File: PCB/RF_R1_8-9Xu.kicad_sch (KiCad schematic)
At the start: 30 parts, among them J1 JST, J2 JST, SW1 BOOT0, U1 STM32F401CBUx, U2 XC6206PxxxMR, Y1 8 MHz

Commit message: Update and pre-production output
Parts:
- C1: LCSC (none) -> C23733
- C2, C3, C9: LCSC (none) -> C52923
- C4, C5, C6, C7, C8: LCSC (none) -> C307331
- D1: LCSC (none) -> C2827688
- F1: LCSC (none) -> C70076
- J1: LCSC (none) -> C265068
- J2: LCSC (none) -> C145956
- R1, R2: LCSC (none) -> C25905
- R10, R11, R12: LCSC (none) -> C25744
- R3, R4, R5, R6, R7, R9: LCSC (none) -> C25076
- R8: LCSC (none) -> C25741
- SW1: footprint Connector_PinHeader_2.54mm:PinHeader_1x02_P2.54mm_Vertical -> Connector_PinHeader_1.27mm:PinHeader_1x02_P1.27mm_Vertical
- U1: LCSC (none) -> C118825
- U2: LCSC (none) -> C5446
- USB1: LCSC (none) -> C165948
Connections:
- net AMUX_SEL_0: now also U1.40 (PB4); no longer U1.42 (PB6)
- net AMUX_SEL_2: now also U1.42 (PB6); no longer U1.40 (PB4)
- net APLEX_EN_PIN_1: now also U1.16 (PA6); no longer U1.39 (PB3)
- net D+: now also D1.3 (I/O2); no longer D1.2 (I/O1)
- net D-: now also D1.2 (I/O1); no longer D1.3 (I/O2)
- net DISCHARGE_PIN: now also U1.14 (PA4); no longer U1.16 (PA6)
- net ROW2: now also R9.1; no longer R3.2
- net ROW3: now also R4.1; no longer R5.2
- net ROW4: now also R5.2; no longer R4.1, R9.1
- net at R3.1: now also U1.25 (PB12); no longer U1.18 (PB0)
- net at R9.2: now also U1.27 (PB14)
- net at U1.17 (PA7): no longer R5.1
- net at U1.19 (PB1): no longer R4.2
- net at U1.26 (PB13): now also R4.2
- net at U1.28 (PB15): now also R5.1
- new net ROW5: R3.2
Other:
- moved on the sheet: R3, R4, R5, R9

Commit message: Final PCB Rev
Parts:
- added J3: Conn_01x03, Connector_PinHeader_2.00mm:PinHeader_1x03_P2.00mm_Vertical, symbol Connector_Generic:Conn_01x03
- added J4: Conn_01x03, cipulot_parts:LED_Strip_Pad, symbol Connector_Generic:Conn_01x03
- added U6: SN74AHCT1G125, Package_TO_SOT_SMD:SOT-23-5, symbol cipulot_parts:SN74AHCT1G125
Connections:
- net +5V: now also J3.3 (Pin_3), J4.3 (Pin_3), U6.5 (VCC)
- net GND: now also J3.1 (Pin_1), J4.1 (Pin_1), U6.1 (~{OE}), U6.3 (GND)
- net LED_3V3: now reaches U1.38 (PA15)
- net LED_3V3: now also U6.2 (A)
- new net LED_5V: J3.2 (Pin_2), J4.2 (Pin_2), U6.4 (B)
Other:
- note added: "LED Logic Level Shifter"
- note added: "LED Strip Connector"
- note added: "SMD"
- note added: "THT"
- moved on the sheet: Y1

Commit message: Fix PA9 being used
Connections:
- net at R3.1: now also U1.18 (PB0); no longer U1.25 (PB12)
- net at R6.2: now also U1.28 (PB15); no longer U1.29 (PA8)
- net at R7.1: now also U1.29 (PA8); no longer U1.30 (PA9)
- net at R9.2: now also U1.26 (PB13); no longer U1.27 (PB14)
- net at R4.2: now also U1.25 (PB12); no longer U1.26 (PB13)
- net at R5.1: now also U1.27 (PB14); no longer U1.28 (PB15)
- no-connect marks 2 -> 3
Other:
- moved on the sheet: R3, R4, R5, R6, R7, R9

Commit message: Production files update
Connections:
- no-connect marks 3 -> 16
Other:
- note added: "DO NOT USE"
- note added: "MCU"
- note added: "NOTE"
- note added: "The board is designed around the STM32F4 family of MCUs to allow for easy swap in case a specific SKU is OOS. Here follows a list of tested (by myself) MCUs: - STM32F4 - SMT32F4 - SMT32F4"
- moved on the sheet: C1, R3, R4, R5, R6, R7, R8, R9

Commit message: Update of PCB
Added shielding copper pad for plate electrical connection, along with EMI filtering through capacitor and inductor.
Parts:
- added C1: 100n, Capacitor_SMD:C_0603_1608Metric, symbol Device:C
- added L1: 220 @ 100MHz, 2A, Inductor_SMD:L_0603_1608Metric, symbol Device:L
- renumbered C9 to C10, C1 to C2, C2 to C3, C3 to C4, C4 to C5, C5 to C6, C6 to C7, C7 to C8, C8 to C9, R7 to R4, R8 to R5, R4 to R6, R9 to R7, R5 to R8, R6 to R9, U6 to U2, U2 to U3
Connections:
- net GND: now also C1.2, L1.2
- new net GNDPWR: C1.1, L1.1
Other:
- note added: "The board is designed around the STM32F4 family of MCUs to allow for easy swap in case a specific SKU is OOS. Here follows a list of tested (by myself) MCUs: - STM32F401CBU"
- note removed: "The board is designed around the STM32F4 family of MCUs to allow for easy swap in case a specific SKU is OOS. Here follows a list of tested (by myself) MCUs: - STM32F4 - SMT32F4 - SMT32F4"
- moved on the sheet: D1

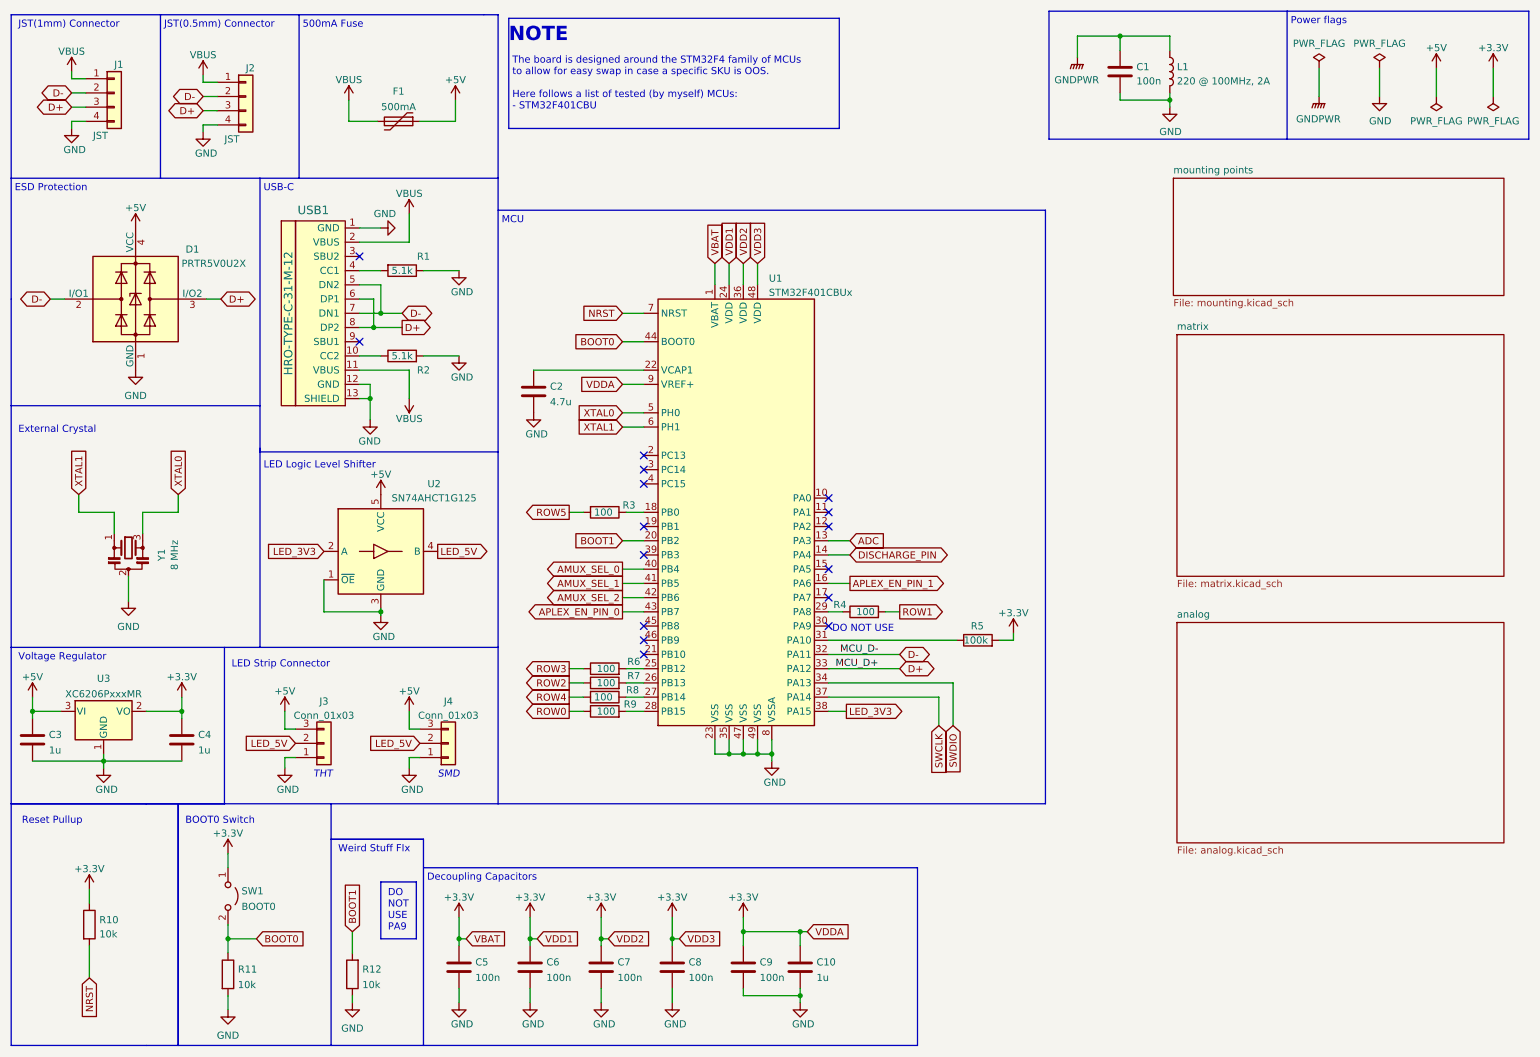
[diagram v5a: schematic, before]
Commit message: Updated files for Rev 1.1
Features added:
- THT LED for Caps Lock and Scroll Lock
- moved filtering components for plate shield to top side
- added filtering components for USB-C shield

Firmware updated accordingly too.
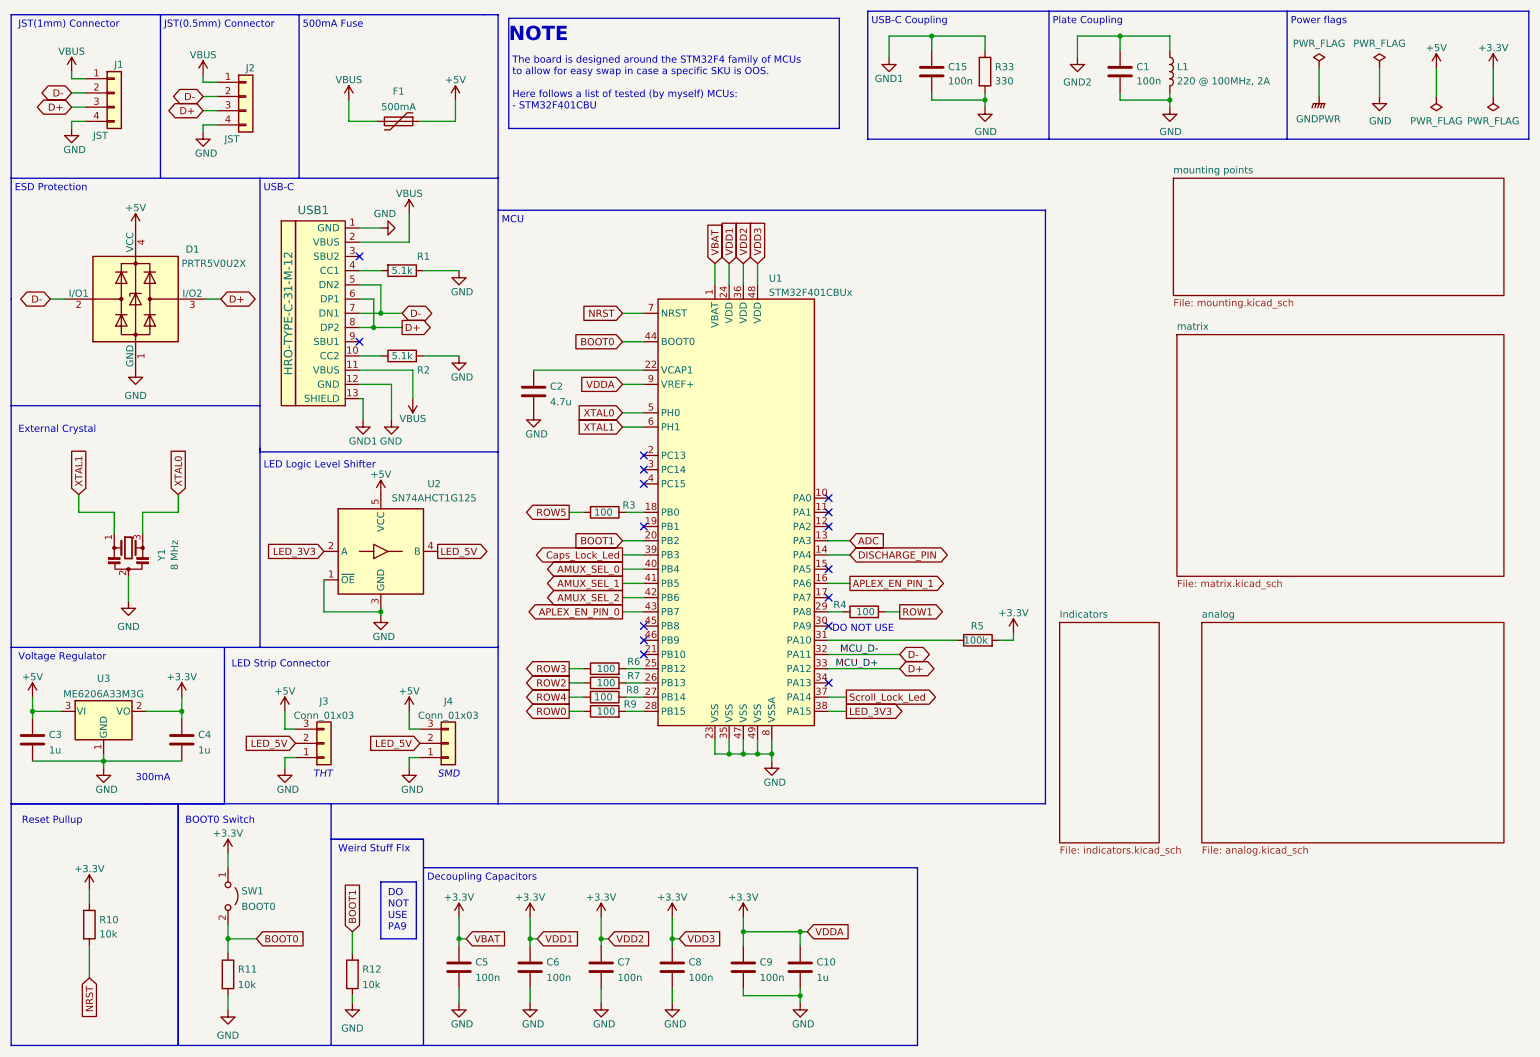
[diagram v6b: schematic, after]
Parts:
- added C15: 100n, Capacitor_SMD:C_0603_1608Metric, symbol Device:C
- added R33: 330, Resistor_SMD:R_0603_1608Metric, symbol Device:R
- U3: value XC6206PxxxMR -> ME6206A33M3G; LCSC C5446 -> C35259
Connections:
- net GND: now also C15.2, R33.2; no longer USB1.13 (SHIELD)
- net GNDPWR: no longer C1.1, L1.1
- net Caps_Lock_Led: now reaches U1.39 (PB3)
- net SWCLK renamed Scroll_Lock_Led
- net SWDIO: no longer names the net of U1.34 (PA13)
- new net GND1: C15.1, R33.1, USB1.13 (SHIELD)
- new net GND2: C1.1, L1.1
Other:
- added sheet Indicators (indicators.kicad_sch)
- note added: "300mA"
- note added: "Plate Coupling"
- note added: "USB-C Coupling"
